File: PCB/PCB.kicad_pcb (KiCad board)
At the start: 4 copper layers, 75 x 75 mm, 148 parts, among them J1 Conn_01x06_Female, J2 5054332681, U1 Hx711, U10 Hx711, U11 Hx711, U12 Hx711, U13 74HC165, U15 LT3042xMSE, U16 74HC165, U2 Hx711, U3 Hx711, U4 Hx711, U5 Hx711, U6 Hx711, U7 Hx711, U8 Hx711, U9 Hx711

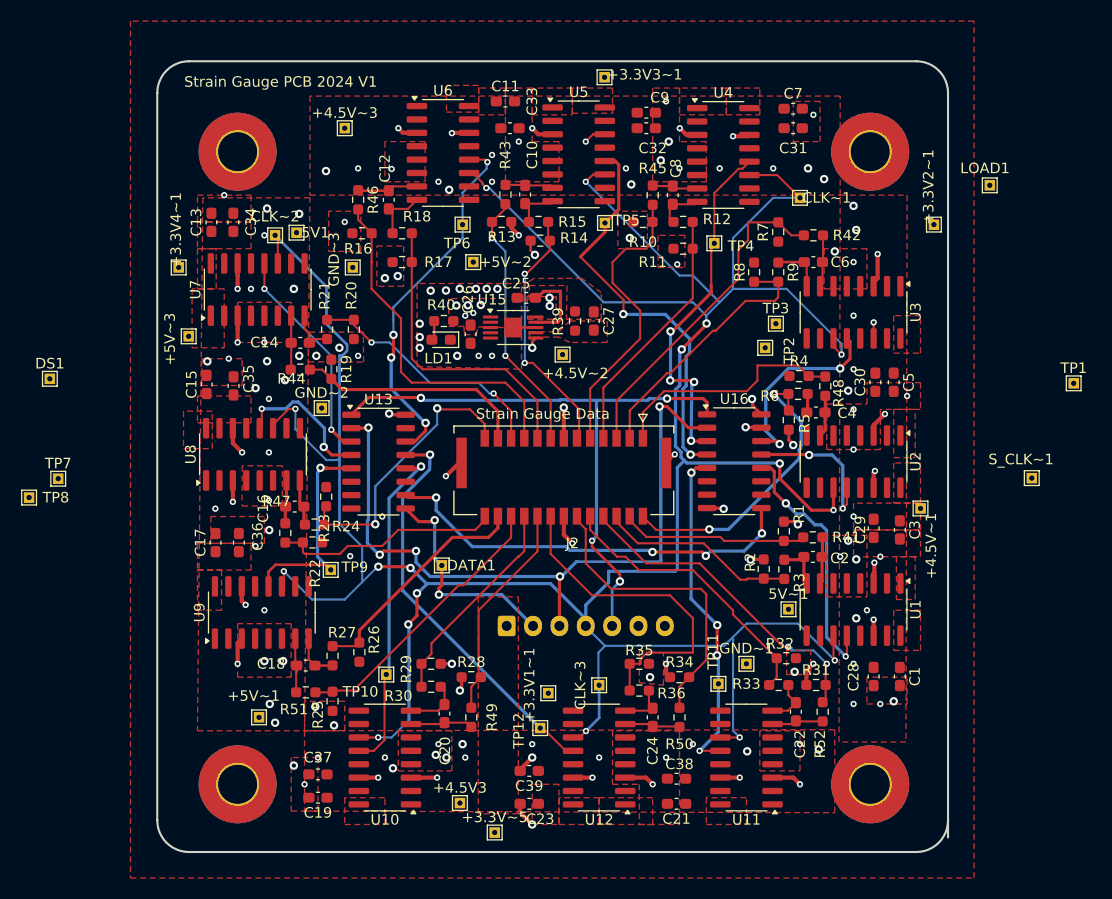
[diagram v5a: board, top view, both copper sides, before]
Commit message: PCB Review feedback implemented
All traces applied, test points moved, voltages are available. Test points have been clustered together on the schematic. Silkscreen passes DRC as to wire tolerances.
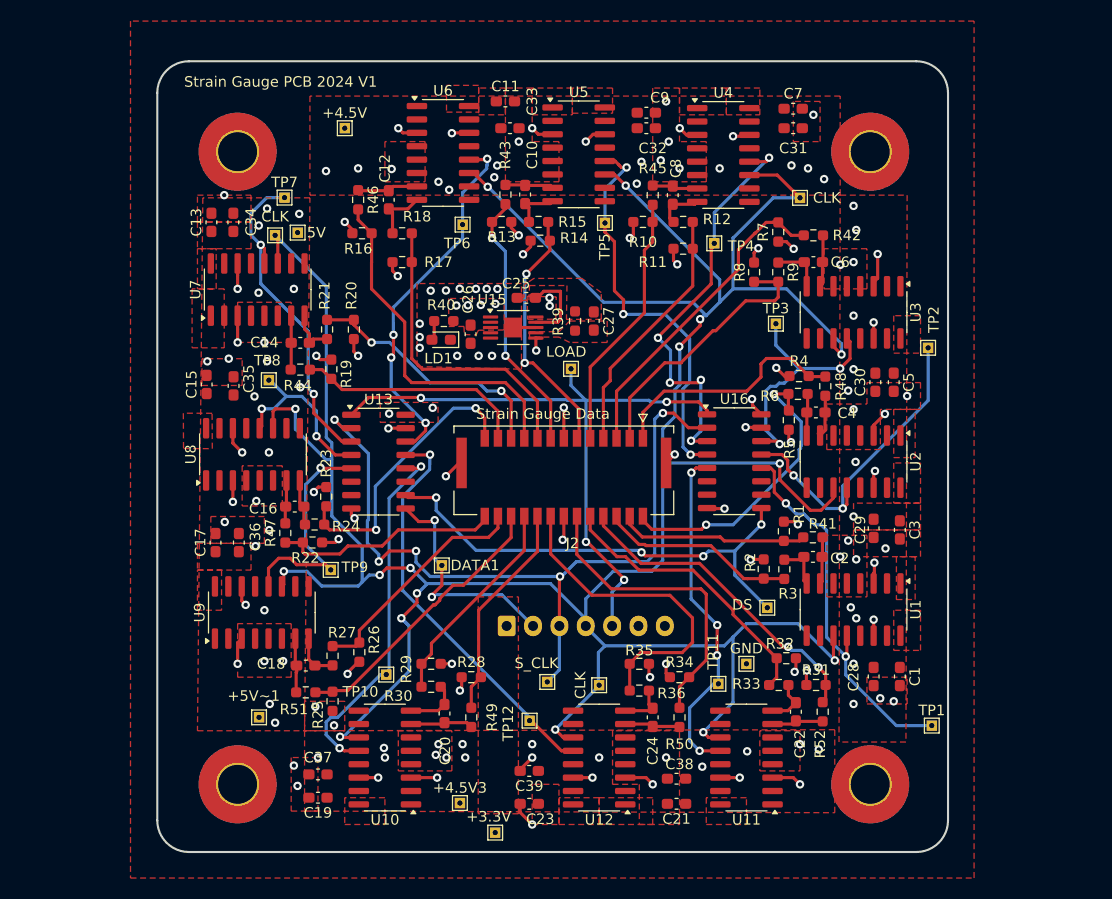
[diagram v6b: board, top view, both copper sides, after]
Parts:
- removed +3.3V2~1, +3.3V3~1, +3.3V4~1, +3.3V~5: 3.3V, TestPoint:TestPoint_THTPad_1.0x1.0mm_Drill0.5mm
- removed +4.5V~1, +4.5V~2: 4.5V, TestPoint:TestPoint_THTPad_1.0x1.0mm_Drill0.5mm
- removed +5V~2, +5V~3, 5V~1: 5V, TestPoint:TestPoint_THTPad_1.0x1.0mm_Drill0.5mm
- removed GND~2, GND~3: GND, TestPoint:TestPoint_THTPad_1.0x1.0mm_Drill0.5mm
- moved DS 71.4 mm to (266.1, 135.7)
- moved S_CLK 49.9 mm to (245.3, 142.7)
- moved LOAD 43.4 mm to (247.5, 113.0)
- moved TP1 35.1 mm to (281.7, 146.8)
- moved TP7 34.2 mm to (220.3, 96.8)
- moved TP8 25.3 mm to (218.9, 114.1)
- moved TP2 15.5 mm to (281.4, 111.0)
- moved +3.3V 14.1 mm to (240.3, 157.0), turned to -90 degrees
- moved TP12 1.23 mm to (243.6, 146.4)
- moved 5V 0.10 mm to (221.6, 100.1)
- renumbered +3.3V1~1 to +3.3V, +4.5V~3 to +4.5V, 5V1 to 5V, CLK~3 to CLK, CLK~2 to CLK, CLK~1 to CLK, DS1 to DS, GND~1 to GND, LOAD1 to LOAD, S_CLK~1 to S_CLK
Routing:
- net GND: track 50.2 -> 74.4 mm, vias 85 -> 89
- net /DOUT12: track 14.4 -> 31.1 mm
- net /DOUT: track 24.5 -> 36.5 mm
- net /DOUT3: track 20.8 -> 31.8 mm
- net /S_CLK: track 69.1 -> 75.4 mm
- net Net-(U13-DS): track 40.3 -> 46.3 mm
- net /DOUT9: track 33.9 -> 39.2 mm, vias 4 -> 5
- net /DOUT1: track 19.7 -> 24.9 mm
- net /DOUT13: track 31.8 -> 35.3 mm, vias 1 -> 2
- net /LOAD: track 58.9 -> 62.3 mm
- net /H9P: track 27.9 -> 24.6 mm
- net /DOUT11: track 14.0 -> 16.9 mm
- net Net-(U2-INA+): track 1.79 -> 3.98 mm
- net /DOUT4: track 21.9 -> 23.0 mm
- net /H12N: track 30.2 -> 29.1 mm
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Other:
- outline, holes or cut-outs redrawn
- board text added: "CLK"
- board text removed: "HX_CLK"

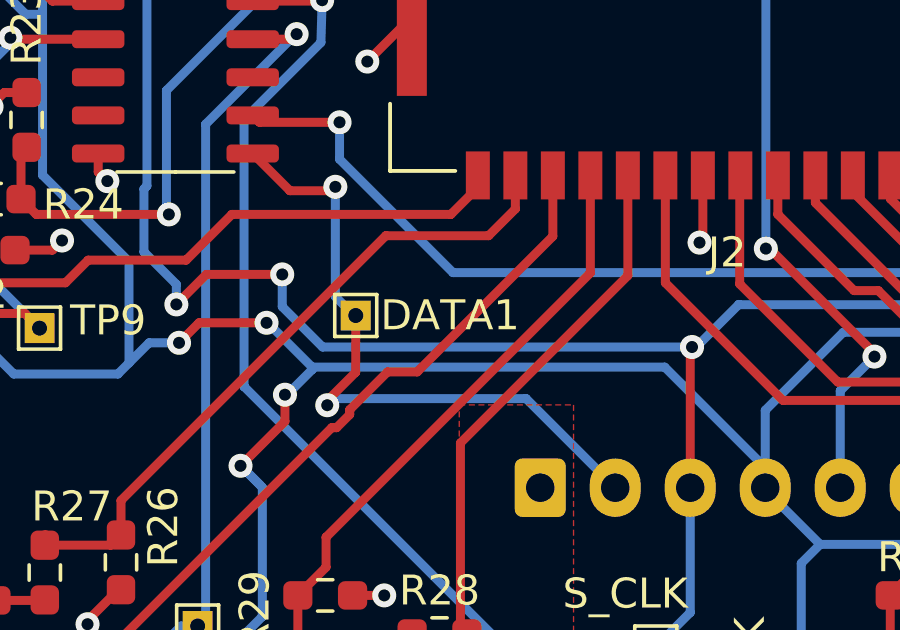
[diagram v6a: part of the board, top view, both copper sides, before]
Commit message: Silkscreen updated
Data1 changed to Data
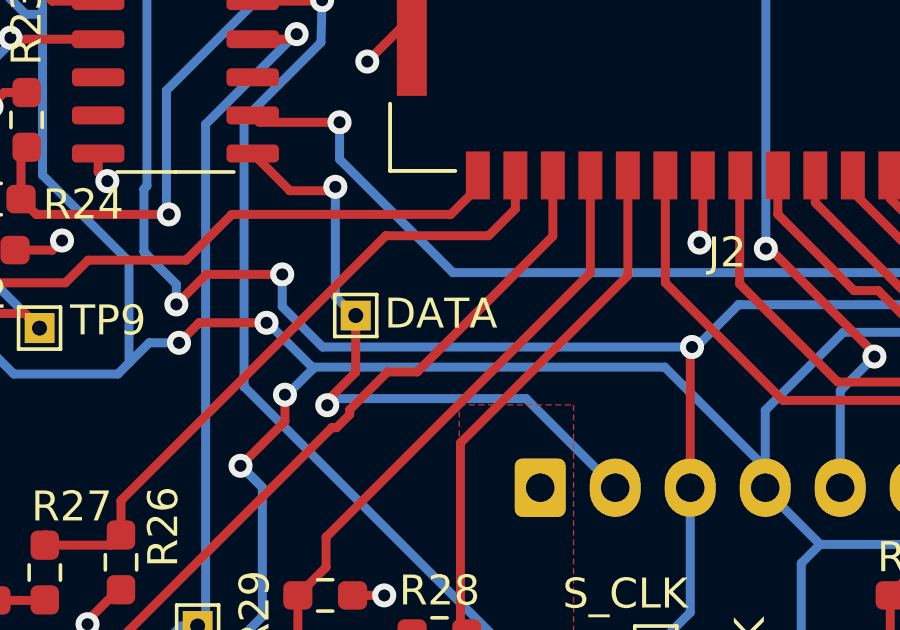
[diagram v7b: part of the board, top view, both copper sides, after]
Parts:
- renumbered DATA1 to DATA
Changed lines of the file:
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@@
 		(descr "THT rectangular pad as test Point, square 1.0mm side length, hole diameter 0.5mm")
 		(tags "test point THT pad rectangle square")
-		(property "Reference" "DATA1"
-			(at 3.142 -0.004 0)
+		(property "Reference" "DATA"
+			(at 2.84 -0.06 0)
 			(layer "F.SilkS")
 			(effects

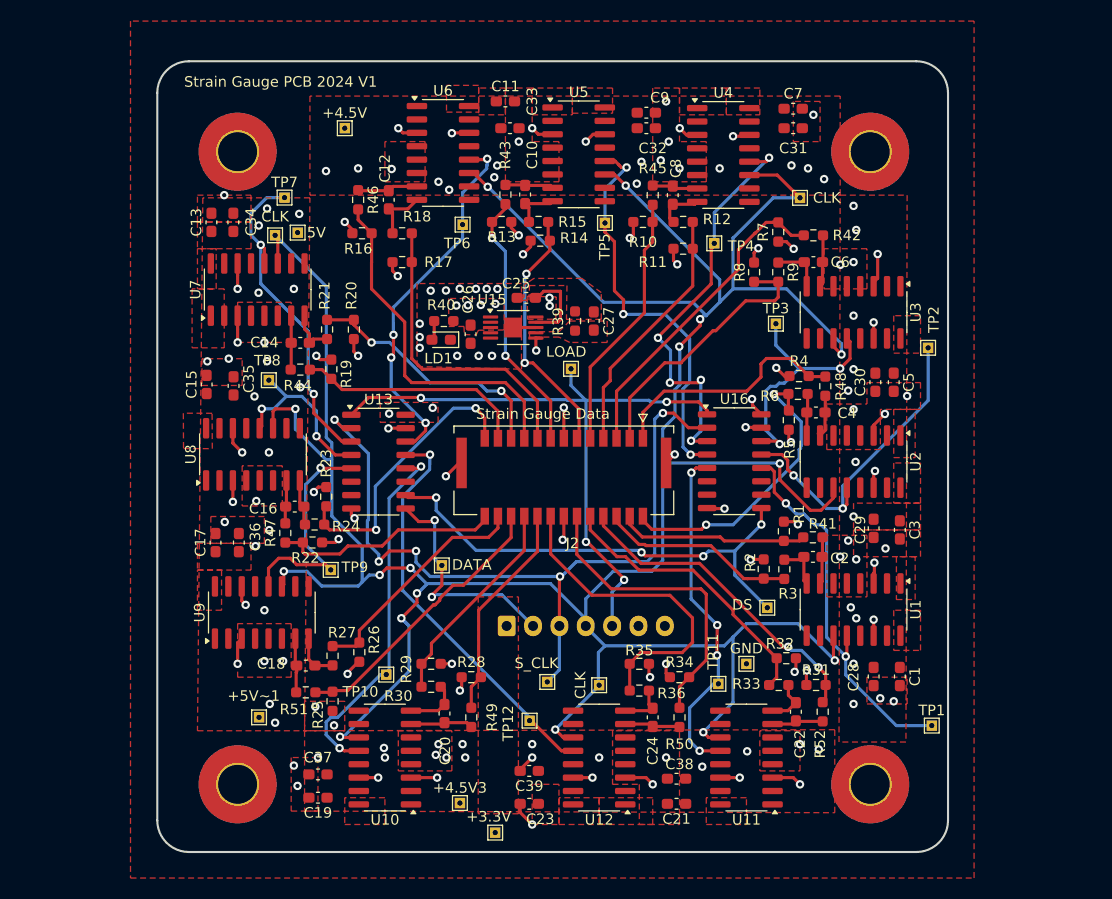
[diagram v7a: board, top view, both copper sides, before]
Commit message: Addressed via feedback
Due to the feedback about vias, they were changed to follow recommendations.
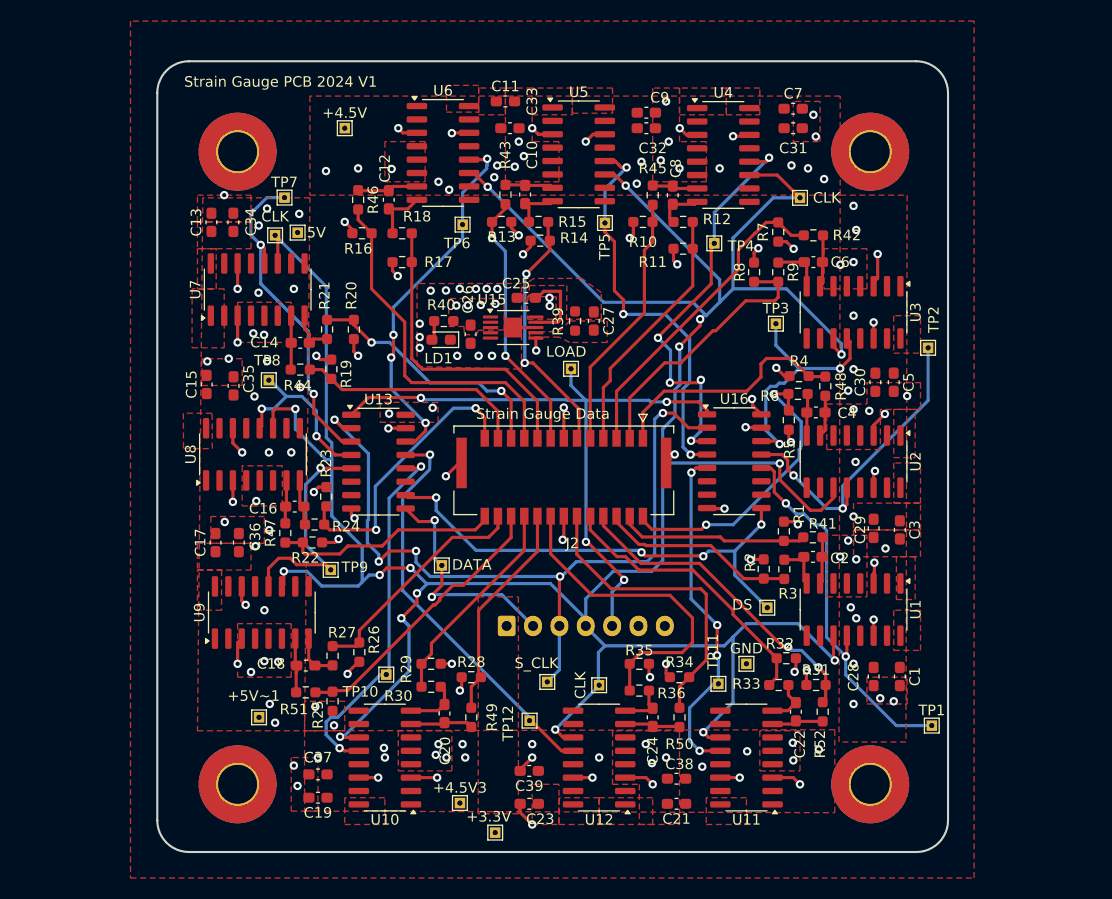
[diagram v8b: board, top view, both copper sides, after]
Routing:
- net GND: vias 89 -> 98
- net +5V: vias 55 -> 56
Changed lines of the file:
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@@
 	)
 	(via
-		(at 220.218 140.716)
+		(at 219.75 140.78)
+		(size 0.8)
+		(drill 0.4)
+		(layers "F.Cu" "B.Cu")
+		(free yes)
+		(net 1)
+	)
+	(via
+		(at 242.19 93.82)
 		(size 0.8)
 		(drill 0.4)
@@
 	)
 	(via
+		(at 217.17 141.75)
+		(size 0.8)
+		(drill 0.4)
+		(layers "F.Cu" "B.Cu")
+		(free yes)
+		(net 1)
+	)
+	(via
 		(at 262.89 90.932)
 		(size 0.8)
@@
 	)
 	(via
+		(at 243.05 92.82)
+		(size 0.8)
+		(drill 0.4)
+		(layers "F.Cu" "B.Cu")
+		(free yes)
+		(net 1)
+	)
+	(via
 		(at 279.4 115.57)
 		(size 0.8)
@@
 	)
 	(via
+		(at 268.61 150.13)
+		(size 0.8)
+		(drill 0.4)
+		(layers "F.Cu" "B.Cu")
+		(free yes)
+		(net 1)
+	)
+	(via
 		(at 226.99 127.16)
 		(size 0.8)
@@
 	)
 	(via
+		(at 255.2 150.39)
+		(size 0.8)
+		(drill 0.4)
+		(layers "F.Cu" "B.Cu")
+		(free yes)
+		(net 1)
+	)
+	(via
 		(at 229.235 151.765)
 		(size 0.8)
@@
 	)
 	(via
-		(at 269.24 148.59)
+		(at 268.56 148.46)
 		(size 0.8)
 		(drill 0.4)
@@
 	)
 	(via
+		(at 254.61 148.58)
+		(size 0.8)
+		(drill 0.4)
+		(layers "F.Cu" "B.Cu")
+		(free yes)
+		(net 1)
+	)
+	(via
 		(at 257.599265 103.080735)
 		(size 0.8)
@@
 	)
 	(via
+		(at 275.81 116.98)
+		(size 0.8)
+		(drill 0.4)
+		(layers "F.Cu" "B.Cu")
+		(free yes)
+		(net 1)
+	)
+	(via
 		(at 213.028 112.284)
 		(size 0.8)
@@
 	)
 	(via
+		(at 217.39 109.63)
+		(size 0.8)
+		(drill 0.4)
+		(layers "F.Cu" "B.Cu")
+		(free yes)
+		(net 1)
+	)
+	(via
 		(at 231.0892 104.1908)
 		(size 0.8)
@@
 	)
 	(via
-		(at 218.44 110.49)
+		(at 218.41 109.77)
 		(size 0.8)
 		(drill 0.4)
@@
 	(via
 		(at 215.06 112.03)
+		(size 0.8)
+		(drill 0.4)
+		(layers "F.Cu" "B.Cu")
+		(free yes)
+		(net 1)
+	)
+	(via
+		(at 270.74 90.96)
 		(size 0.8)
 		(drill 0.4)
@@
 		(net 2)
 	)
+	(via
+		(at 220.99 120.92)
+		(size 0.8)
+		(drill 0.4)
+		(layers "F.Cu" "B.Cu")
+		(free yes)
+		(net 2)
+	)
